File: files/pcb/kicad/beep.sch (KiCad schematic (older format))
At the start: 0 parts

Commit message: 回路図更新
温度湿度センサ
大気圧センサ
輝度センサ
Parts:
- added U?: LOAD, symbol LOAD
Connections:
- new net +5V: U?.1 (VCC)
- new net beep: U?.2 (GND)
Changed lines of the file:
@@
 $Descr A4 11693 8268
 encoding utf-8
-Sheet 1 12
+Sheet 7 12
 Title ""
 Date "23 aug 2014"
@@
 Comment4 ""
 $EndDescr
+$Comp
+L LOAD U?
+U 1 1 53F901A9
+P 5750 3950
+F 0 "U?" H 5830 3710 39  0000 C CNN
+F 1 "LOAD" H 5630 3710 39  0000 C CNN
+F 2 "" H 5750 3950 60  0000 C CNN
+F 3 "" H 5750 3950 60  0000 C CNN
+	1    5750 3950
+	1    0    0    -1
+$EndComp
+Text HLabel 5750 4550 3    60   Input ~ 0
+beep
+$Comp
+L +5V #PWR?
+U 1 1 53F901C9
+P 5750 3400
+F 0 "#PWR?" H 5750 3490 20  0001 C CNN
+F 1 "+5V" H 5750 3490 30  0000 C CNN
+F 2 "" H 5750 3400 60  0000 C CNN
+F 3 "" H 5750 3400 60  0000 C CNN
+	1    5750 3400
+	1    0    0    -1
+$EndComp
+Wire Wire Line
+	5750 3450 5750 3400
+Wire Wire Line
+	5750 4450 5750 4550
 $EndSCHEMATC

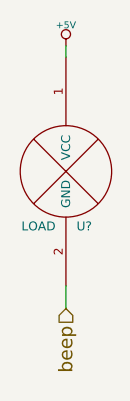
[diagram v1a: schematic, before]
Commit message: 回路図更新、DS1307対応
バスの接続が未
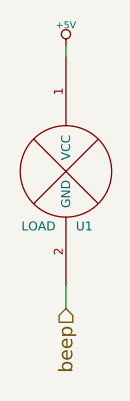
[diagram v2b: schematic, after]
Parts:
- gave numbers to parts that had none: 1
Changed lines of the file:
@@
 $Descr A4 11693 8268
 encoding utf-8
-Sheet 7 12
+Sheet 7 13
 Title ""
-Date "23 aug 2014"
+Date "24 aug 2014"
 Rev ""
 Comp ""
@@
 $EndDescr
 $Comp
-L LOAD U?
+L LOAD U1
 U 1 1 53F901A9
 P 5750 3950
-F 0 "U?" H 5830 3710 39  0000 C CNN
+F 0 "U1" H 5830 3710 39  0000 C CNN
 F 1 "LOAD" H 5630 3710 39  0000 C CNN
 F 2 "" H 5750 3950 60  0000 C CNN
@@
 beep
 $Comp
-L +5V #PWR?
+L +5V #PWR46
 U 1 1 53F901C9
 P 5750 3400
-F 0 "#PWR?" H 5750 3490 20  0001 C CNN
+F 0 "#PWR46" H 5750 3490 20  0001 C CNN
 F 1 "+5V" H 5750 3490 30  0000 C CNN
 F 2 "" H 5750 3400 60  0000 C CNN

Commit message: 部品リスト・パッケージライブラリを更新
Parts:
- renumbered U1 to U12
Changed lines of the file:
@@
 $EndDescr
 $Comp
-L LOAD U1
+L LOAD U12
 U 1 1 53F901A9
 P 5750 3950
-F 0 "U1" H 5830 3710 39  0000 C CNN
+F 0 "U12" H 5830 3710 39  0000 C CNN
 F 1 "LOAD" H 5630 3710 39  0000 C CNN
 F 2 "" H 5750 3950 60  0000 C CNN
@@
 beep
 $Comp
-L +5V #PWR054
+L +5V #PWR057
 U 1 1 53F901C9
 P 5750 3400
-F 0 "#PWR054" H 5750 3490 20  0001 C CNN
+F 0 "#PWR057" H 5750 3490 20  0001 C CNN
 F 1 "+5V" H 5750 3490 30  0000 C CNN
 F 2 "" H 5750 3400 60  0000 C CNN
